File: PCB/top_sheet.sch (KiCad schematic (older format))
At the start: 4 parts

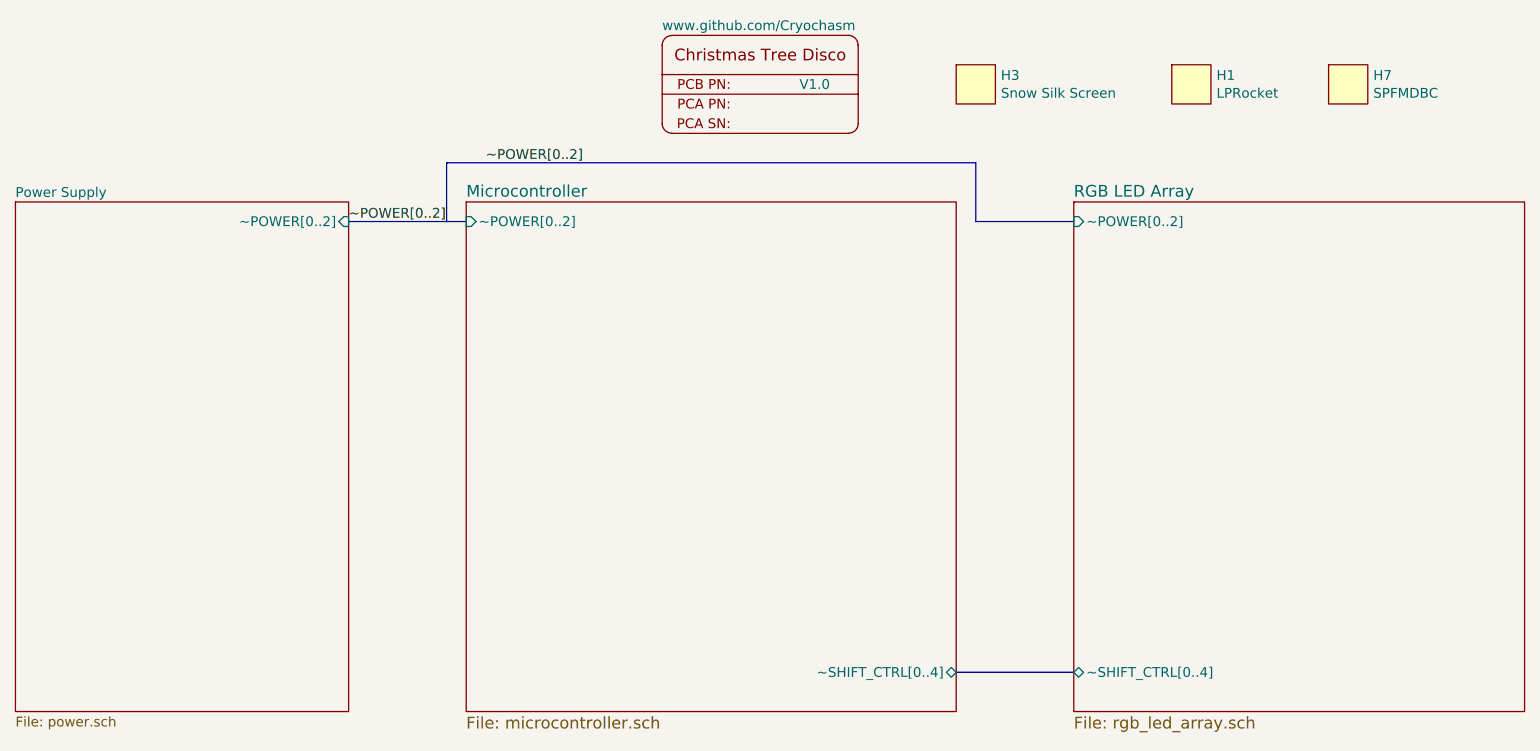
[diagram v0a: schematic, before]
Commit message: Footprint Modifications
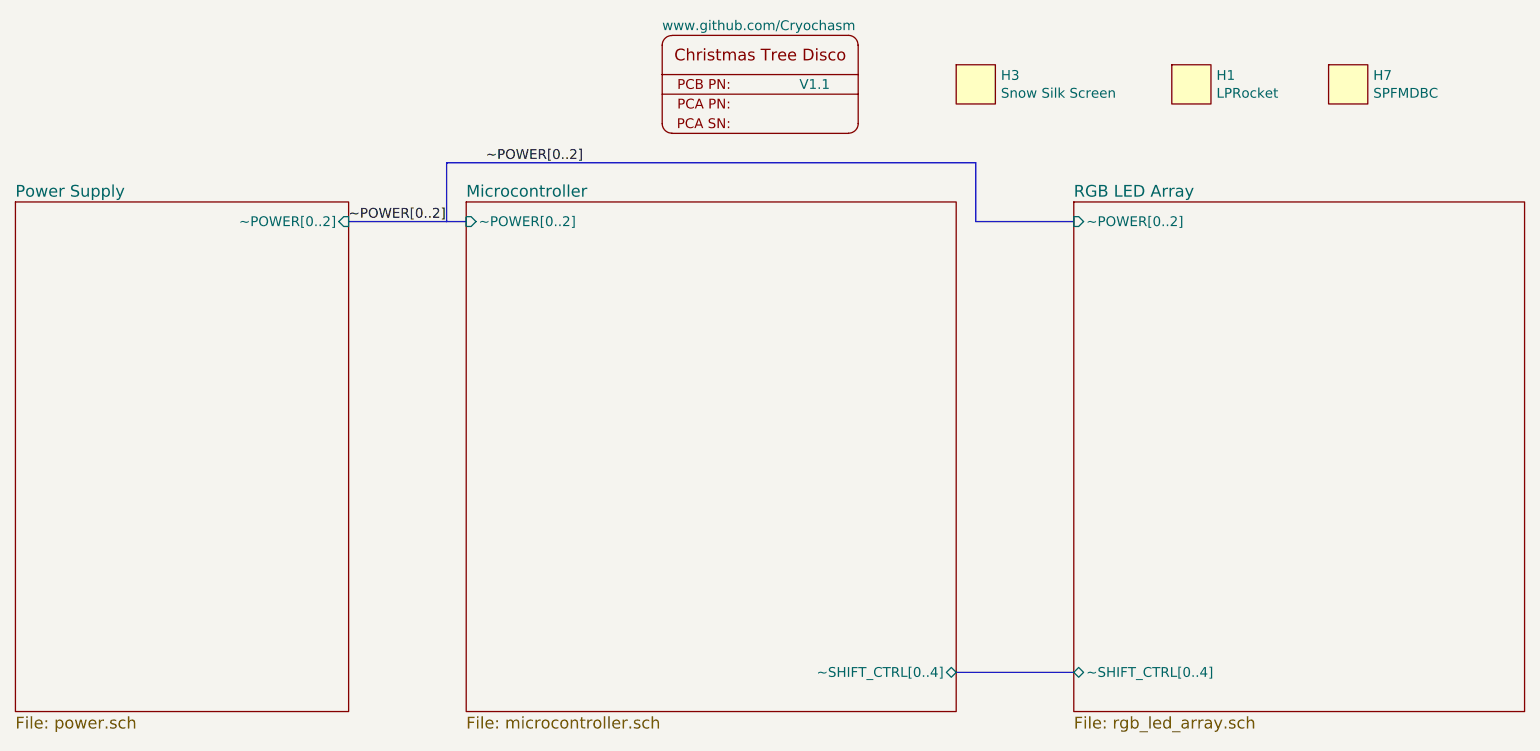
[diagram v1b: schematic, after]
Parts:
- renumbered V1.0 to V1.1
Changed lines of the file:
@@
 Sheet 2 20
 Title "Christmas Tree Disco"
-Date "2017-08-23"
-Rev "V1.0"
+Date "2017-09-10"
+Rev "V1.1"
 Comp "www.GitHub.com/Cryochasm"
 Comment1 ""
@@
 $EndSheet
 $Comp
-L PCB_LABEL V1.0
+L PCB_LABEL V1.1
 U 1 1 59822887
 P 5000 2100
-F 0 "V1.0" H 5200 2200 50  0000 L CNN
+F 0 "V1.1" H 5200 2200 50  0000 L CNN
 F 1 "www.github.com/Cryochasm" H 4500 2500 50  0000 L CNN
 F 2 "local:Cryochasm" H 5150 1900 60  0001 C CNN
@@
 S 1200 2600 1700 2600
 U 5984D7F4
-F0 "Power Supply" 50
-F1 "power.sch" 50
+F0 "Power Supply" 60
+F1 "power.sch" 60
 F2 "~~POWER[0..2]" I R 2900 2700 50
 $EndSheet

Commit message: Schematic V2
REQUIRES CHANGE TO SOFTWARE: Changed pin of LAT from D7 to D0 to avoid
using the non-maskable interrupt pin.

Added a SMD LED D8 to provide and enviornmental lighting effect.

Removed power supply circuit; USB power from the dev board is sufficent
for
LED brightness. Must be plugged into USB 3.0 or a 2A rated supply.

Updated symbol library to use KiBOM and to Lib Version 4.

TODO: Update  PCB
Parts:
- H1, H3, H7: symbol Generic -> local:Generic; Config (none) -> Do Not Fit; Included in BOM No -> (none)
- V2.0: renamed from V1.1; symbol PCB_LABEL -> local:PCB_LABEL; Config (none) -> Do Not Fit; Included in BOM No -> (none)
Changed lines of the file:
@@
-EESchema Schematic File Version 2
+EESchema Schematic File Version 4
 LIBS:local
 LIBS:Christmas_Tree_Disco-cache
@@
 $Descr A 11000 8500
 encoding utf-8
-Sheet 2 20
+Sheet 2 19
 Title "Christmas Tree Disco"
-Date "2017-09-10"
-Rev "V1.1"
+Date "2017-09-20"
+Rev "V2"
 Comp "www.GitHub.com/Cryochasm"
 Comment1 ""
@@
 $EndSheet
 $Comp
-L PCB_LABEL V1.1
+L local:PCB_LABEL V2.0
 U 1 1 59822887
 P 5000 2100
-F 0 "V1.1" H 5200 2200 50  0000 L CNN
+F 0 "V2.0" H 5200 2200 50  0000 L CNN
 F 1 "www.github.com/Cryochasm" H 4500 2500 50  0000 L CNN
 F 2 "local:Cryochasm" H 5150 1900 60  0001 C CNN
@@
 F 4 "-" H 5000 2100 60  0001 C CNN "MPN"
 F 5 "-" H 5000 2100 60  0001 C CNN "Description"
-F 6 "No" H 5000 2100 60  0001 C CNN "Included in BOM"
+F 6 "Do Not Fit" H 5000 2100 60  0001 C CNN "Config"
 	1    5000 2100
 	1    0    0    -1
 $EndComp
-$Sheet
-S 1200 2600 1700 2600
-U 5984D7F4
-F0 "Power Supply" 60
-F1 "power.sch" 60
-F2 "~~POWER[0..2]" I R 2900 2700 50
-$EndSheet
-Wire Bus Line
-	2900 2700 3500 2700
 Wire Bus Line
 	3400 2700 3400 2400
@@
 	6000 5000 6600 5000
 $Comp
-L Generic H3
+L local:Generic H3
 U 1 1 5987C99A
 P 6100 2000
@@
 F 4 "-" H 6100 1700 50  0001 C CNN "MPN"
 F 5 "-" H 6100 1600 50  0001 C CNN "Description"
-F 6 "No" H 6100 1500 50  0001 C CNN "Included in BOM"
+F 6 "Do Not Fit" H 6100 1500 50  0001 C CNN "Config"
 	1    6100 2000
 	1    0    0    -1
 $EndComp
-Text Label 2900 2700 0    50   ~ 0
-~~POWER[0..2]
 $Comp
-L Generic H1
+L local:Generic H1
 U 1 1 598A6860
 P 7200 2000
@@
 F 4 "-" H 7200 1600 50  0001 C CNN "Description"
 F 5 "-" H 7200 1700 50  0001 C CNN "MPN"
-F 6 "No" H 7200 1500 50  0001 C CNN "Included in BOM"
+F 6 "Do Not Fit" H 7200 1500 50  0001 C CNN "Config"
 	1    7200 2000
 	1    0    0    -1
 $EndComp
 $Comp
-L Generic H7
+L local:Generic H7
 U 1 1 59934D6E
 P 8000 2000
@@
 F 4 "-" H 8000 1700 50  0001 C CNN "MPN"
 F 5 "-" H 8000 1600 50  0001 C CNN "Description"
-F 6 "No" H 8000 1500 50  0001 C CNN "Included in BOM"
+F 6 "Do Not Fit" H 8000 1500 50  0001 C CNN "Config"
 	1    8000 2000
 	1    0    0    -1
 $EndComp
+Wire Bus Line
+	3500 2700 3400 2700
 $EndSCHEMATC
